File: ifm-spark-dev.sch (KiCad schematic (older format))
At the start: 16 parts

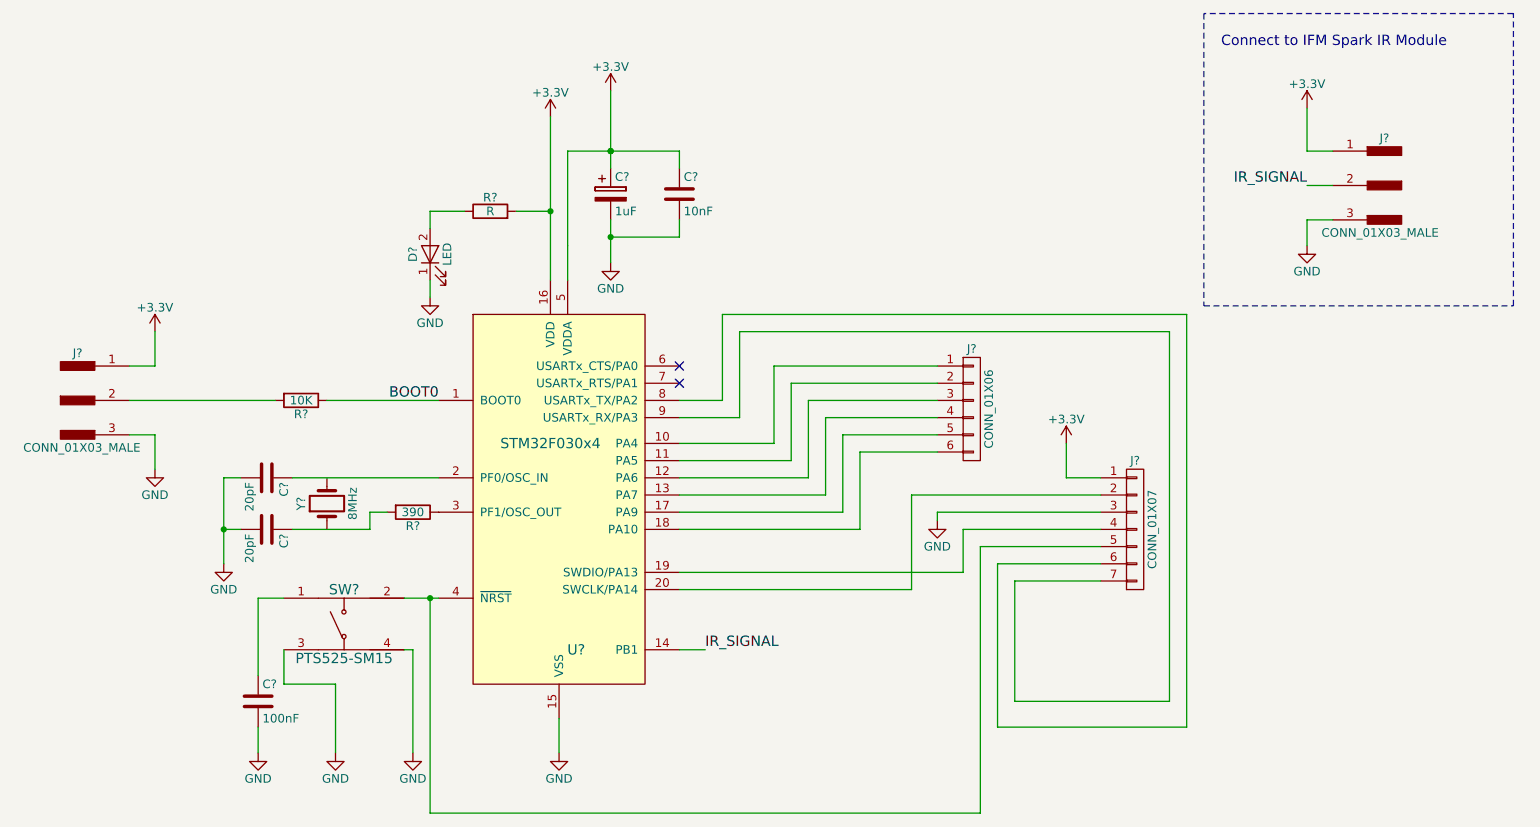
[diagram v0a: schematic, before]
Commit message: Add net names to the ST-Link pins and connect the other two pins
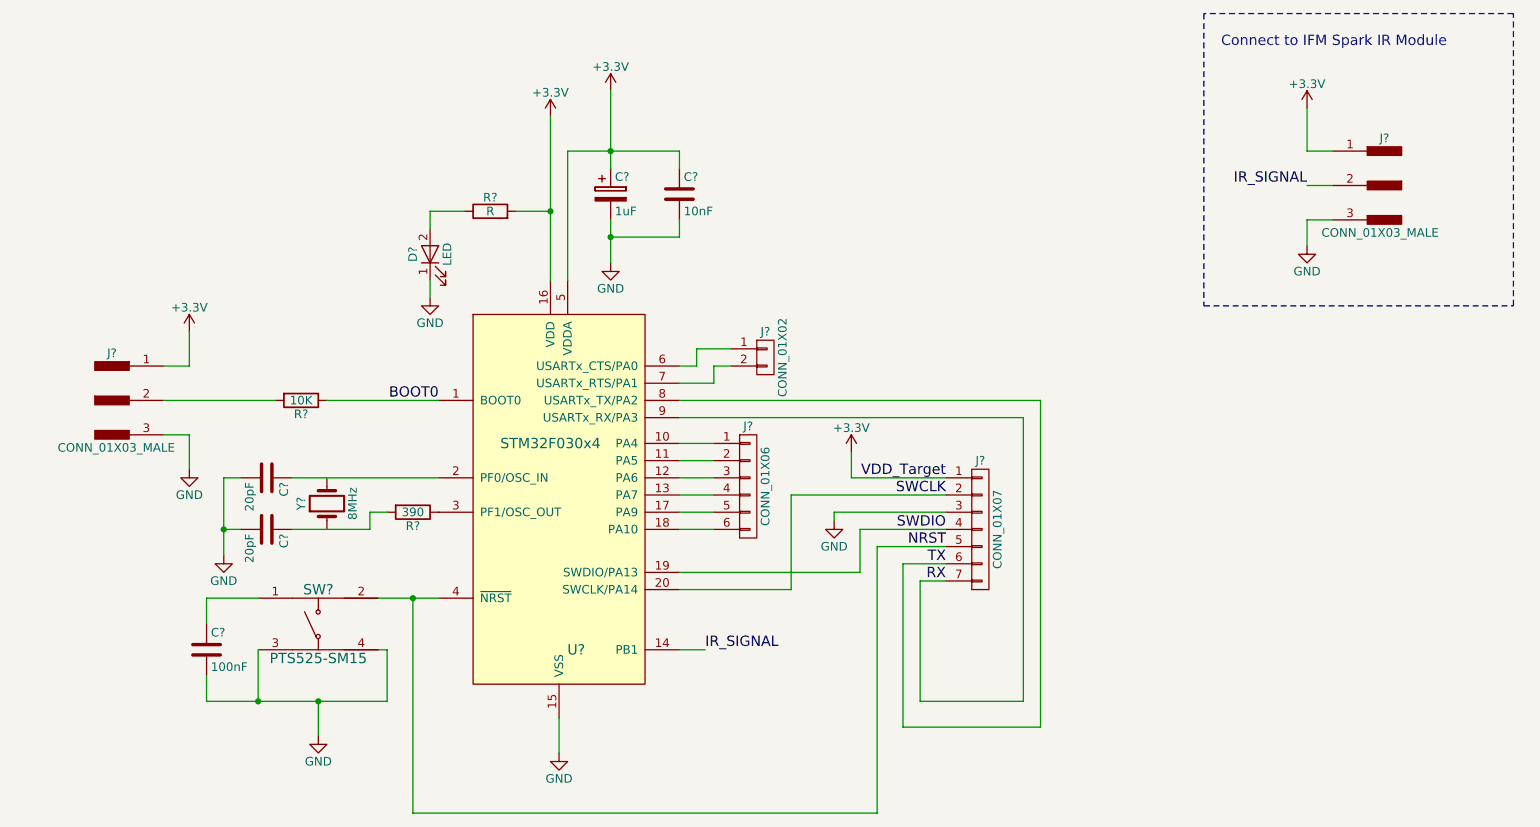
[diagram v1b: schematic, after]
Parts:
- added J?: CONN_01X02, symbol CONN_01X02
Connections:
- net SWDIO: now reaches J?.4 (P4), U?.19 (SWDIO/PA13)
- net SWCLK: now reaches J?.2 (P2), U?.20 (SWCLK/PA14)
- net NRST: now reaches J?.5 (P5), SW?.2, U?.4 (~NRST)
- net at U?.6 (USARTx_CTS/PA0): now also J?.1 (P1)
- net at U?.7 (USARTx_RTS/PA1): now also J?.2 (P2)
- net TX: now reaches J?.6 (P6), U?.8 (USARTx_TX/PA2)
- net RX: now reaches J?.7 (P7), U?.9 (USARTx_RX/PA3)
- no-connect marks 2 -> 0
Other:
- moved on the sheet: C?, J?, SW?

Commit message: Add data fields for tactile switch
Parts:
- SW?: DKPN (none) -> CKN9104CT-ND; MPN (none) -> PTS525SM15SMTR2 LFS
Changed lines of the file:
@@
 F 1 "PTS525-SM15" H 4150 4000 60  0000 C CNN
 F 2 "" H 4150 4200 60  0001 C CNN
-F 3 "" H 4150 4200 60  0001 C CNN
+F 3 "http://www.ckswitches.com/media/1467/pts525.pdf" H 4150 4200 60  0001 C CNN
+F 4 "PTS525SM15SMTR2 LFS" H 4150 4200 60  0001 C CNN "MPN"
+F 5 "CKN9104CT-ND" H 4150 4200 60  0001 C CNN "DKPN"
 	1    4150 4200
 	1    0    0    -1

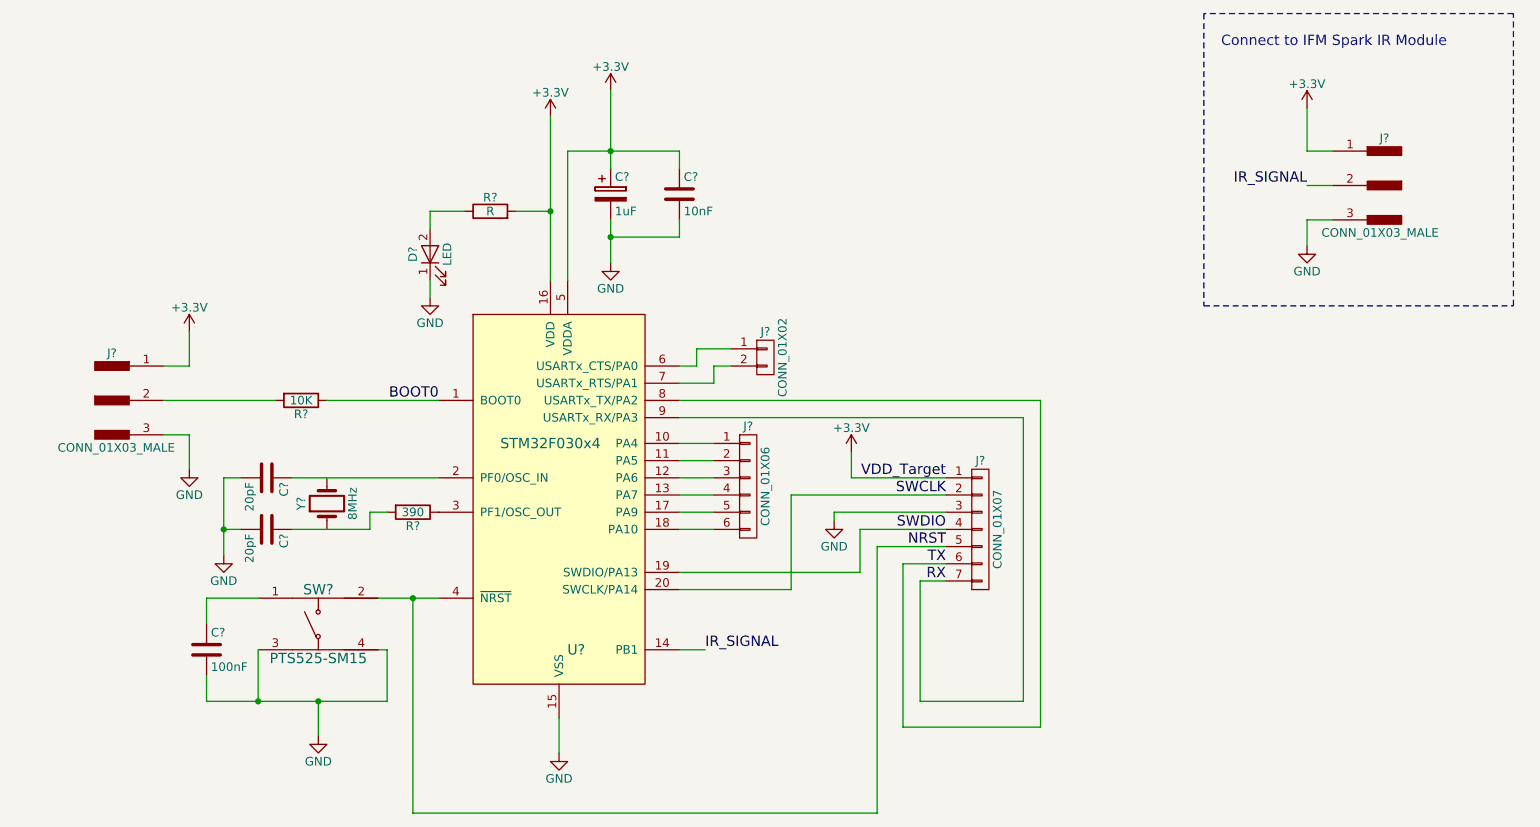
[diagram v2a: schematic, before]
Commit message: Added an LED to PA4 and a pull-up to the switch
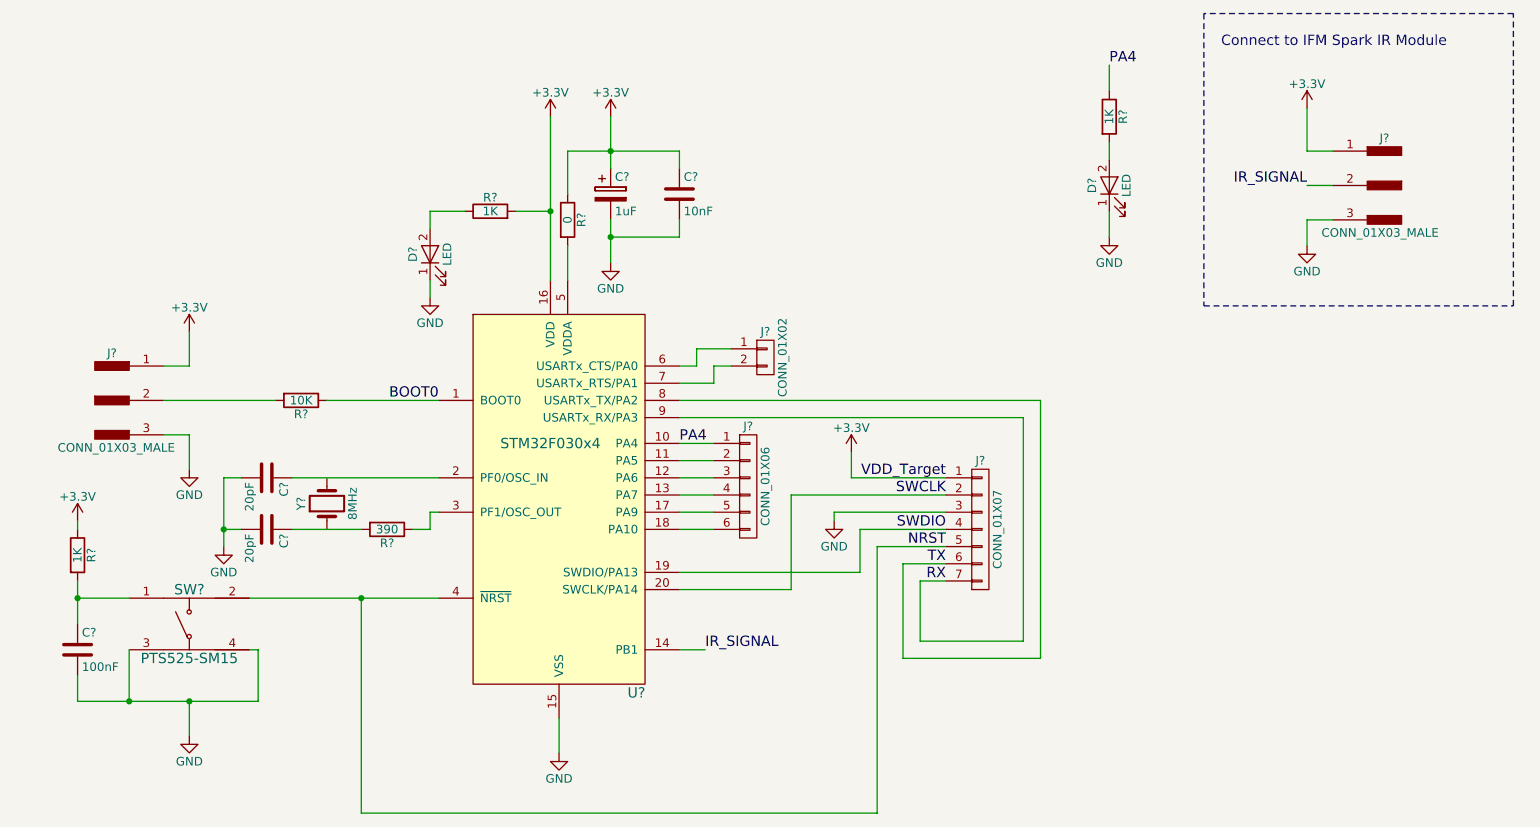
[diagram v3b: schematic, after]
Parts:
- added D?: LED, symbol LED
- added R?: 0, symbol R
- added R? (x2): 1K, symbol R
- R?: value R -> 1K
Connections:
- net +3V3: now also R?.1, R?.1; no longer U?.5 (VDDA)
- net GND: now also D?.1 (K)
- net PA4: now reaches J?.1 (P1), U?.10 (PA4)
- net PA4: now also R?.1
- net at C?.1, SW?.1: now also R?.2
- new net: R?.2, U?.5 (VDDA)
- new net: D?.2 (A), R?.2
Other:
- moved on the sheet: C?, R?, SW?
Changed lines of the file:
@@
 U 1 1 59251F3D
 P 5550 3500
-F 0 "U?" H 5650 2650 60  0000 C CNN
+F 0 "U?" H 6000 2400 60  0000 C CNN
 F 1 "STM32F030x4" H 5500 3850 60  0000 C CNN
 F 2 "" H 5550 3700 60  0001 C CNN
@@
 L GND #PWR?
 U 1 1 5925217D
-P 3600 3800
-F 0 "#PWR?" H 3600 3550 50  0001 C CNN
-F 1 "GND" H 3600 3650 50  0000 C CNN
-F 2 "" H 3600 3800 50  0001 C CNN
-F 3 "" H 3600 3800 50  0001 C CNN
-	1    3600 3800
+P 3600 3750
+F 0 "#PWR?" H 3600 3500 50  0001 C CNN
+F 1 "GND" H 3600 3600 50  0000 C CNN
+F 2 "" H 3600 3750 50  0001 C CNN
+F 3 "" H 3600 3750 50  0001 C CNN
+	1    3600 3750
 	1    0    0    -1
 $EndComp
@@
 	3600 3350 3600 3650
 Wire Wire Line
-	3600 3650 3600 3800
+	3600 3650 3600 3750
 Wire Wire Line
 	3700 3650 3600 3650
@@
 	4000 3350 4850 3350
 Wire Wire Line
-	4000 3650 4450 3650
-Wire Wire Line
-	4450 3650 4450 3550
-Wire Wire Line
-	4450 3550 4550 3550
+	4000 3650 4400 3650
 Text Label 6400 4350 0    60   ~ 0
 IR_SIGNAL
@@
 $EndComp
 Wire Wire Line
-	5850 1100 5850 1450
+	5850 1250 5850 1450
 Wire Wire Line
 	5850 1450 5850 1550
@@
 L +3.3V #PWR?
 U 1 1 5929A588
-P 5850 1100
-F 0 "#PWR?" H 5850 950 50  0001 C CNN
-F 1 "+3.3V" H 5850 1240 50  0000 C CNN
-F 2 "" H 5850 1100 50  0001 C CNN
-F 3 "" H 5850 1100 50  0001 C CNN
-	1    5850 1100
+P 5850 1250
+F 0 "#PWR?" H 5850 1100 50  0001 C CNN
+F 1 "+3.3V" H 5850 1390 50  0000 C CNN
+F 2 "" H 5850 1250 50  0001 C CNN
+F 3 "" H 5850 1250 50  0001 C CNN
+	1    5850 1250
 	1    0    0    -1
 $EndComp
@@
 L R R?
 U 1 1 5929A77F
-P 4700 3550
-F 0 "R?" V 4780 3550 50  0000 C CNN
-F 1 "390" V 4700 3550 50  0000 C CNN
-F 2 "" V 4630 3550 50  0001 C CNN
-F 3 "" H 4700 3550 50  0001 C CNN
-	1    4700 3550
+P 4550 3650
+F 0 "R?" V 4630 3650 50  0000 C CNN
+F 1 "390" V 4550 3650 50  0000 C CNN
+F 2 "" V 4480 3650 50  0001 C CNN
+F 3 "" H 4550 3650 50  0001 C CNN
+	1    4550 3650
 	0    1    1    0
 $EndComp
@@
 L PTS525-SM15 SW?
 U 1 1 592A4BF6
-P 4150 4200
-F 0 "SW?" H 4150 4400 60  0000 C CNN
-F 1 "PTS525-SM15" H 4150 4000 60  0000 C CNN
-F 2 "" H 4150 4200 60  0001 C CNN
-F 3 "http://www.ckswitches.com/media/1467/pts525.pdf" H 4150 4200 60  0001 C CNN
-F 4 "PTS525SM15SMTR2 LFS" H 4150 4200 60  0001 C CNN "MPN"
-F 5 "CKN9104CT-ND" H 4150 4200 60  0001 C CNN "DKPN"
-	1    4150 4200
-	1    0    0    -1
-$EndComp
-Wire Wire Line
-	4500 4050 4700 4050
-Wire Wire Line
-	4700 4050 4850 4050
+P 3400 4200
+F 0 "SW?" H 3400 4400 60  0000 C CNN
+F 1 "PTS525-SM15" H 3400 4000 60  0000 C CNN
+F 2 "" H 3400 4200 60  0001 C CNN
+F 3 "http://www.ckswitches.com/media/1467/pts525.pdf" H 3400 4200 60  0001 C CNN
+F 4 "PTS525SM15SMTR2 LFS" H 3400 4200 60  0001 C CNN "MPN"
+F 5 "CKN9104CT-ND" H 3400 4200 60  0001 C CNN "DKPN"
+	1    3400 4200
+	1    0    0    -1
+$EndComp
+Wire Wire Line
+	3750 4050 4400 4050
+Wire Wire Line
+	4400 4050 4850 4050
 $Comp
 L C C?
 U 1 1 592A4D64
-P 3500 4350
-F 0 "C?" H 3525 4450 50  0000 L CNN
-F 1 "100nF" H 3525 4250 50  0000 L CNN
-F 2 "" H 3538 4200 50  0001 C CNN
-F 3 "" H 3500 4350 50  0001 C CNN
-	1    3500 4350
+P 2750 4350
+F 0 "C?" H 2775 4450 50  0000 L CNN
+F 1 "100nF" H 2775 4250 50  0000 L CNN
+F 2 "" H 2788 4200 50  0001 C CNN
+F 3 "" H 2750 4350 50  0001 C CNN
+	1    2750 4350
 	1    0    0    -1
 $EndComp
@@
 L GND #PWR?
 U 1 1 592A4E5A
-P 4150 4850
-F 0 "#PWR?" H 4150 4600 50  0001 C CNN
-F 1 "GND" H 4150 4700 50  0000 C CNN
-F 2 "" H 4150 4850 50  0001 C CNN
-F 3 "" H 4150 4850 50  0001 C CNN
-	1    4150 4850
+P 3400 4850
+F 0 "#PWR?" H 3400 4600 50  0001 C CNN
+F 1 "GND" H 3400 4700 50  0000 C CNN
+F 2 "" H 3400 4850 50  0001 C CNN
+F 3 "" H 3400 4850 50  0001 C CNN
+	1    3400 4850
 	1    0    0    -1
 $EndComp
@@
 	3250 2900 3900 2900
 Wire Wire Line
-	3800 4050 3500 4050
-Wire Wire Line
-	3500 4050 3500 4200
-Wire Wire Line
-	4500 4350 4550 4350
-Wire Wire Line
-	4550 4650 4550 4350
+	3050 4050 2750 4050
+Wire Wire Line
+	2750 3950 2750 4050
+Wire Wire Line
+	2750 4050 2750 4200
+Wire Wire Line
+	3750 4350 3800 4350
+Wire Wire Line
+	3800 4650 3800 4350
 $Comp
 L CONN_01X03_MALE J?
@@
 	7400 3750 7400 5300
 Wire Wire Line
-	7400 5300 4700 5300
-Wire Wire Line
-	4700 5300 4700 4050
-Connection ~ 4700 4050
+	7400 5300 4400 5300
+Wire Wire Line
+	4400 5300 4400 4050
+Connection ~ 4400 4050
 Wire Wire Line
 	7800 3850 7550 3850
 Wire Wire Line
-	7550 3850 7550 4800
-Wire Wire Line
-	7550 4800 8350 4800
-Wire Wire Line
-	8350 4800 8350 2900
+	7550 3850 7550 4400
+Wire Wire Line
+	7550 4400 8350 4400
+Wire Wire Line
+	8350 4400 8350 2900
 Wire Wire Line
 	8350 2900 6250 2900
@@
 	7800 3950 7650 3950
 Wire Wire Line
-	7650 3950 7650 4650
-Wire Wire Line
-	7650 4650 8250 4650
-Wire Wire Line
-	8250 4650 8250 3000
+	7650 3950 7650 4300
+Wire Wire Line
+	7650 4300 8250 4300
+Wire Wire Line
+	8250 4300 8250 3000
 Wire Wire Line
 	8250 3000 6250 3000
-Wire Wire Line
-	5600 1450 5600 2200
 $Comp
 L CONN_01X06 J?
@@
 P 5150 1800
 F 0 "R?" V 5230 1800 50  0000 C CNN
-F 1 "R" V 5150 1800 50  0000 C CNN
+F 1 "1K" V 5150 1800 50  0000 C CNN
 F 2 "" V 5080 1800 50  0001 C CNN
 F 3 "" H 5150 1800 50  0001 C CNN
@@
 	6450 2700 6550 2700
 Wire Wire Line
-	3500 4500 3500 4650
-Wire Wire Line
-	3500 4650 3800 4650
-Wire Wire Line
-	3800 4650 4150 4650
-Wire Wire Line
-	4150 4650 4550 4650
-Wire Wire Line
-	4150 4850 4150 4650
-Connection ~ 4150 4650
-Wire Wire Line
-	3800 4350 3800 4650
-Connection ~ 3800 4650
+	2750 4500 2750 4650
+Wire Wire Line
+	2750 4650 3050 4650
+Wire Wire Line
+	3050 4650 3400 4650
+Wire Wire Line
+	3400 4650 3800 4650
+Wire Wire Line
+	3400 4850 3400 4650
+Connection ~ 3400 4650
+Wire Wire Line
+	3050 4350 3050 4650
+Connection ~ 3050 4650
 Text Label 7800 3350 2    60   ~ 0
 VDD_Target
@@
 Text Label 7800 3950 2    60   ~ 0
 RX
+$Comp
+L R R?
+U 1 1 594E146B
+P 5600 1850
+F 0 "R?" V 5680 1850 50  0000 C CNN
+F 1 "0" V 5600 1850 50  0000 C CNN
+F 2 "" V 5530 1850 50  0001 C CNN
+F 3 "" H 5600 1850 50  0001 C CNN
+	1    5600 1850
+	1    0    0    -1
+$EndComp
+Wire Wire Line
+	5600 1450 5600 1700
+Wire Wire Line
+	5600 2200 5600 2000
+$Comp
+L R R?
+U 1 1 594E20A6
+P 2750 3800
+F 0 "R?" V 2830 3800 50  0000 C CNN
+F 1 "1K" V 2750 3800 50  0000 C CNN
+F 2 "" V 2680 3800 50  0001 C CNN
+F 3 "" H 2750 3800 50  0001 C CNN
+	1    2750 3800
+	1    0    0    -1
+$EndComp
+$Comp
+L +3.3V #PWR?
+U 1 1 594E214F
+P 2750 3600
+F 0 "#PWR?" H 2750 3450 50  0001 C CNN
+F 1 "+3.3V" H 2750 3740 50  0000 C CNN
+F 2 "" H 2750 3600 50  0001 C CNN
+F 3 "" H 2750 3600 50  0001 C CNN
+	1    2750 3600
+	1    0    0    -1
+$EndComp
+Wire Wire Line
+	2750 3600 2750 3650
+Connection ~ 2750 4050
+Text Label 6250 3150 0    60   ~ 0
+PA4
+Text Label 8750 950  0    60   ~ 0
+PA4
+$Comp
+L R R?
+U 1 1 594E286C
+P 8750 1250
+F 0 "R?" V 8830 1250 50  0000 C CNN
+F 1 "1K" V 8750 1250 50  0000 C CNN
+F 2 "" V 8680 1250 50  0001 C CNN
+F 3 "" H 8750 1250 50  0001 C CNN
+	1    8750 1250
+	1    0    0    -1
+$EndComp
+$Comp
+L LED D?
+U 1 1 594E28B5
+P 8750 1650
+F 0 "D?" H 8750 1750 50  0000 C CNN
+F 1 "LED" H 8750 1550 50  0000 C CNN
+F 2 "" H 8750 1650 50  0001 C CNN
+F 3 "" H 8750 1650 50  0001 C CNN
+	1    8750 1650
+	0    -1   -1   0
+$EndComp
+$Comp
+L GND #PWR?
+U 1 1 594E29ED
+P 8750 1950
+F 0 "#PWR?" H 8750 1700 50  0001 C CNN
+F 1 "GND" H 8750 1800 50  0000 C CNN
+F 2 "" H 8750 1950 50  0001 C CNN
+F 3 "" H 8750 1950 50  0001 C CNN
+	1    8750 1950
+	1    0    0    -1
+$EndComp
+Wire Wire Line
+	8750 1950 8750 1800
+Wire Wire Line
+	8750 1500 8750 1400
+Wire Wire Line
+	8750 1100 8750 950
+Wire Wire Line
+	4850 3550 4800 3550
+Wire Wire Line
+	4800 3550 4800 3650
+Wire Wire Line
+	4800 3650 4700 3650
 $EndSCHEMATC
